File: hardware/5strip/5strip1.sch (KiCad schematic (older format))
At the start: 48 parts, among them K1 CONN_3, P1 CONN_4, P2 USB_MICRO-B, P3 CONN_4, P4 CONN_2, P5 CONN_4, P6 CONN_6, P7 CONN_6, Q1 NPN, U1 FT232R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

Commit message: Added some new hardware, included some code objects forgotten locally.
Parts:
- removed JP2: JUMPER3, ~, symbol JUMPER3
- removed JP3, JP4, JP5: JUMPER, ~, symbol JUMPER
- removed K1: CONN_3, symbol CONN_3
- removed P6: CONN_6, symbol CONN_6
- removed R13, R14: R, ~, symbol R
- removed U1: FT232R, symbol FT232R
- added C11, C12: 1µF, ~, symbol C
- added C? (x2): CP, ~, symbol CP
- added P6, P7: CONN_4, ~, symbol CONN_4
- added U1: FT230X, ~, symbol FT230X
- renumbered P7 to P8
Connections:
- net labels added: B4, B5, DEBUG_LED, G4, G5, LB4, LB5, LG4, LG5, LR4, LR5, R4, R5
- net labels removed: PULLUP, SCL, SDA
- wire segments 115 -> 108
- no-connect marks 6 -> 22
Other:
- note added: "TIMER T15C1"
- note added: "TIMER T15C2"
- note added: "TIMER T16C1"
- note added: "TIMER T17C1"
- note added: "TIMER T1C1\n"
- note added: "TIMER T1C2n\n"
- note added: "TIMER T1C3n"
- note added: "TIMER T1C4\n\n"
- note added: "TIMER T2C1"
- note added: "TIMER T2C2\n"
- note added: "TIMER T2C3\n"
- note added: "TIMER T2C4\n"
- note added: "TIMER T3C1\n"
- note added: "TIMER T3C2\n"
- note added: "TIMER T3C3"
- note added: "TIMER T3C4"
- note removed: "I2C Bus"

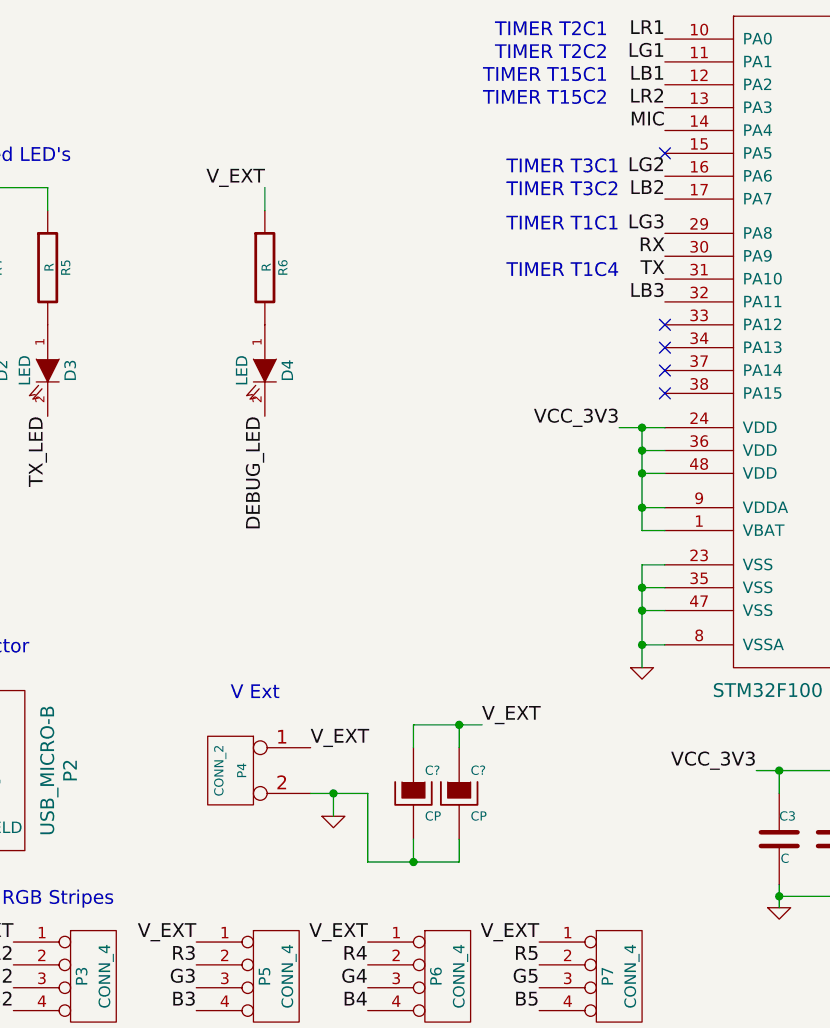
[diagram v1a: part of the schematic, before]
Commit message: Updated timer registers in rxlamp code
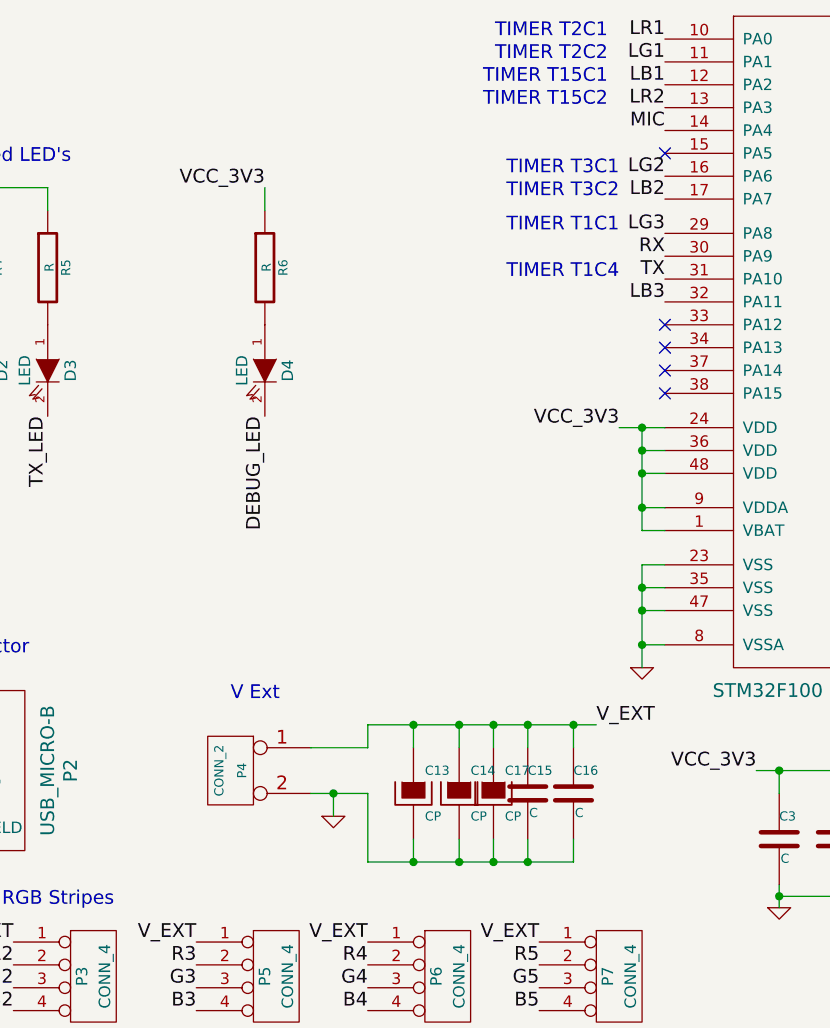
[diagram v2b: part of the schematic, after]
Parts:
- added C15, C16: C, ~, symbol C
- added C17: CP, ~, symbol CP
- gave numbers to parts that had none: 2
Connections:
- net GND: now also C15.2, C16.2, C17.2
- net VCC_3V3: now also R6.1
- net V_EXT: now also C15.1, C16.1, C17.1; no longer R6.1
